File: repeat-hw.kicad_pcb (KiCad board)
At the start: 2 copper layers, 1 part, among them U1 nRF5340-QKxx

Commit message: added W5100
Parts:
- added J1: RB1-125BAG1A, Connector_RJ:RJ45_Cetus_J1B1211CCD_Horizontal, F.Cu at (79.7, 53.6)
- added U2: W5100, Package_QFP:LQFP-80_10x10mm_P0.4mm, F.Cu at (83.0, 40.0)
- added Y1: 32MHz, Crystal:Crystal_SMD_3225-4Pin_3.2x2.5mm, F.Cu at (107.9, 35.0)
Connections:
- U1 pad A13: unconnected-(U1-PadA13) -> Net-(C14-Pad1)
- U1 pad A15: unconnected-(U1-PadA15) -> Net-(C12-Pad1)
- U1 pad A21: unconnected-(U1-PadA21) -> Net-(L1-Pad2)
- U1 pad A23: unconnected-(U1-PadA23) -> Net-(C8-Pad1)
- U1 pad A27: unconnected-(U1-PadA27) -> Net-(C11-Pad1)
- U1 pad A5: unconnected-(U1-PadA5) -> Net-(C1-Pad1)
- U1 pad AA1: unconnected-(U1-PadAA1) -> /MCU/NFC2
- U1 pad AC31: unconnected-(U1-PadAC31) -> Net-(C10-Pad1)
- U1 pad B10: unconnected-(U1-PadB10) -> Net-(L3-Pad2)
- U1 pad B2: unconnected-(U1-PadB2) -> /MCU/D+
- U1 pad B30: unconnected-(U1-PadB30) -> Net-(C9-Pad1)
- U1 pad B4: unconnected-(U1-PadB4) -> /MCU/D-
- U1 pad B6: unconnected-(U1-PadB6) -> Net-(C3-Pad1)
- U1 pad C31: unconnected-(U1-PadC31) -> Net-(C4-Pad1)
- U1 pad E1: unconnected-(U1-PadE1) -> VDD
- U1 pad EP: unconnected-(U1-PadEP) -> GND
- U1 pad G31: unconnected-(U1-PadG31) -> Net-(C11-Pad1)
- U1 pad L31: unconnected-(U1-PadL31) -> Net-(C13-Pad1)
- U1 pad W1: unconnected-(U1-PadW1) -> /MCU/NFC1

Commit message: Finishe PoE and ethernet
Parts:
- removed J1: RB1-125BAG1A, Connector_RJ:RJ45_Cetus_J1B1211CCD_Horizontal
- added C1: 4u7, Connector_RJ:RJ45_Cetus_J1B1211CCD_Horizontal, F.Cu at (77.7, 63.0)
- added D2: 1N4148W, Diode_SMD:D_SOD-123, F.Cu at (112.7, 59.5)
- added U3: TLV431DBZ, Package_TO_SOT_SMD:SOT-23, F.Cu at (118.0, 60.0)
- added Y2: 25MHz, Crystal:Crystal_SMD_3225-4Pin_3.2x2.5mm, F.Cu at (112.4, 63.4)
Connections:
- net Net-(U2-Pad10) renamed GNDA
- net Net-(U2-Pad12) renamed +3V3
- net Net-(U2-Pad7) renamed +1V8A
- U2 pad 1: unconnected-(U2-Pad1) -> Net-(U2-Pad1)
- U2 pad 11: unconnected-(U2-Pad11) -> +1V8
- U2 pad 13: Net-(U2-Pad13) -> GND
- U2 pad 14: Net-(U2-Pad13) -> GND
- U2 pad 15: Net-(U2-Pad15) -> +1V8
- U2 pad 16: Net-(U2-Pad15) -> +1V8
- U2 pad 17: Net-(U2-Pad13) -> GND
- U2 pad 2: unconnected-(U2-Pad2) -> +3V3A
- U2 pad 27: unconnected-(U2-Pad27) -> /W5100 + PoE/MISO
- U2 pad 28: unconnected-(U2-Pad28) -> /W5100 + PoE/MOSI
- U2 pad 29: unconnected-(U2-Pad29) -> /W5100 + PoE/~{CS}
- U2 pad 30: unconnected-(U2-Pad30) -> /W5100 + PoE/CLK
- U2 pad 31: unconnected-(U2-Pad31) -> Net-(U2-Pad31)
- U2 pad 32: Net-(U2-Pad13) -> GND
- U2 pad 33: Net-(U2-Pad15) -> +1V8
- U2 pad 34: unconnected-(U2-Pad34) -> GND
- U2 pad 35: unconnected-(U2-Pad35) -> GND
- U2 pad 36: unconnected-(U2-Pad36) -> GND
- U2 pad 37: unconnected-(U2-Pad37) -> GND
- U2 pad 43: Net-(U2-Pad13) -> GND
- U2 pad 5: unconnected-(U2-Pad5) -> /W5100 + PoE/RD+
- U2 pad 56: unconnected-(U2-Pad56) -> /W5100 + PoE/~{INT}
- U2 pad 59: unconnected-(U2-Pad59) -> /W5100 + PoE/~{RST}
- U2 pad 6: unconnected-(U2-Pad6) -> /W5100 + PoE/RD-
- U2 pad 63: unconnected-(U2-Pad63) -> GND
- U2 pad 64: unconnected-(U2-Pad64) -> GND
- U2 pad 65: unconnected-(U2-Pad65) -> GND
- U2 pad 66: unconnected-(U2-Pad66) -> /W5100 + PoE/LINK
- U2 pad 68: Net-(U2-Pad13) -> GND
- U2 pad 69: Net-(U2-Pad15) -> +1V8
- U2 pad 70: unconnected-(U2-Pad70) -> /W5100 + PoE/FDX
- U2 pad 75: unconnected-(U2-Pad75) -> Net-(U2-Pad75)
- U2 pad 76: unconnected-(U2-Pad76) -> Net-(U2-Pad76)
- U2 pad 8: unconnected-(U2-Pad8) -> /W5100 + PoE/TD+
- U2 pad 9: unconnected-(U2-Pad9) -> /W5100 + PoE/TD-

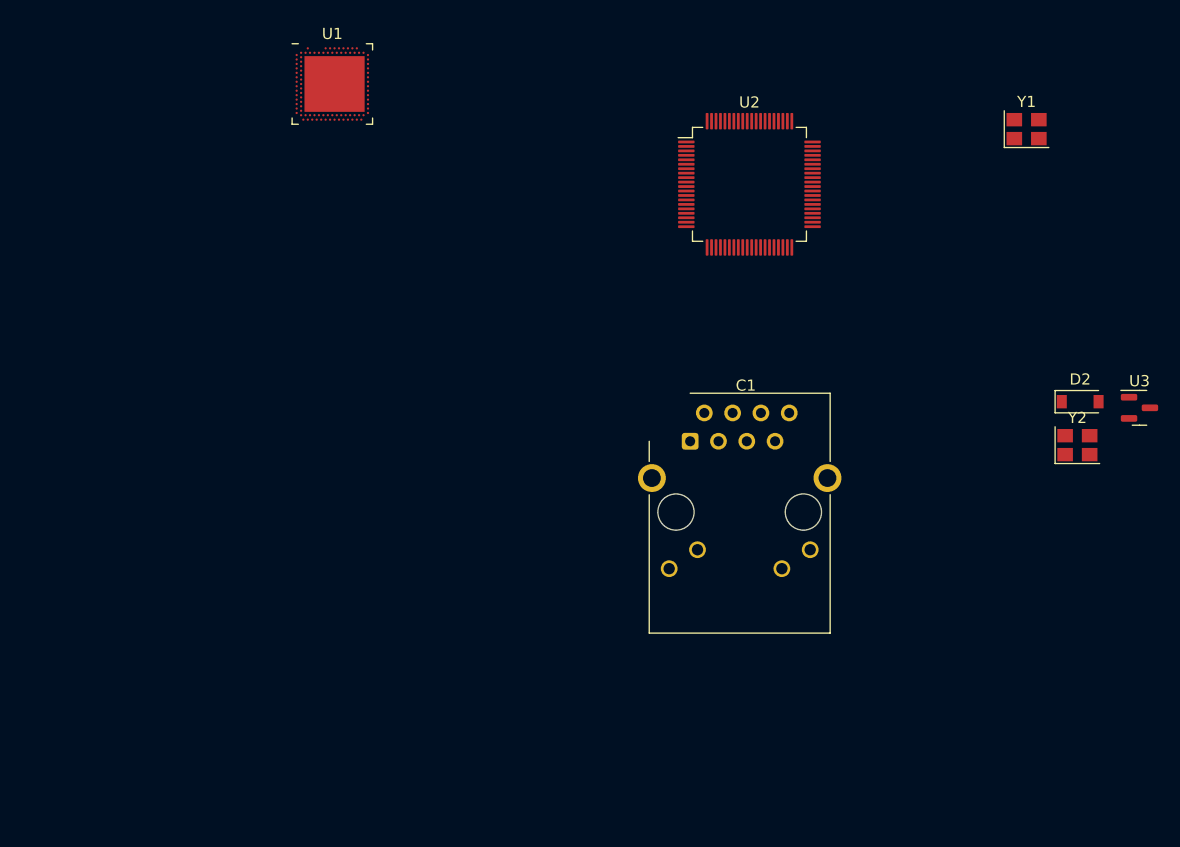
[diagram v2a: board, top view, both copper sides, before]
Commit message: Added USB port
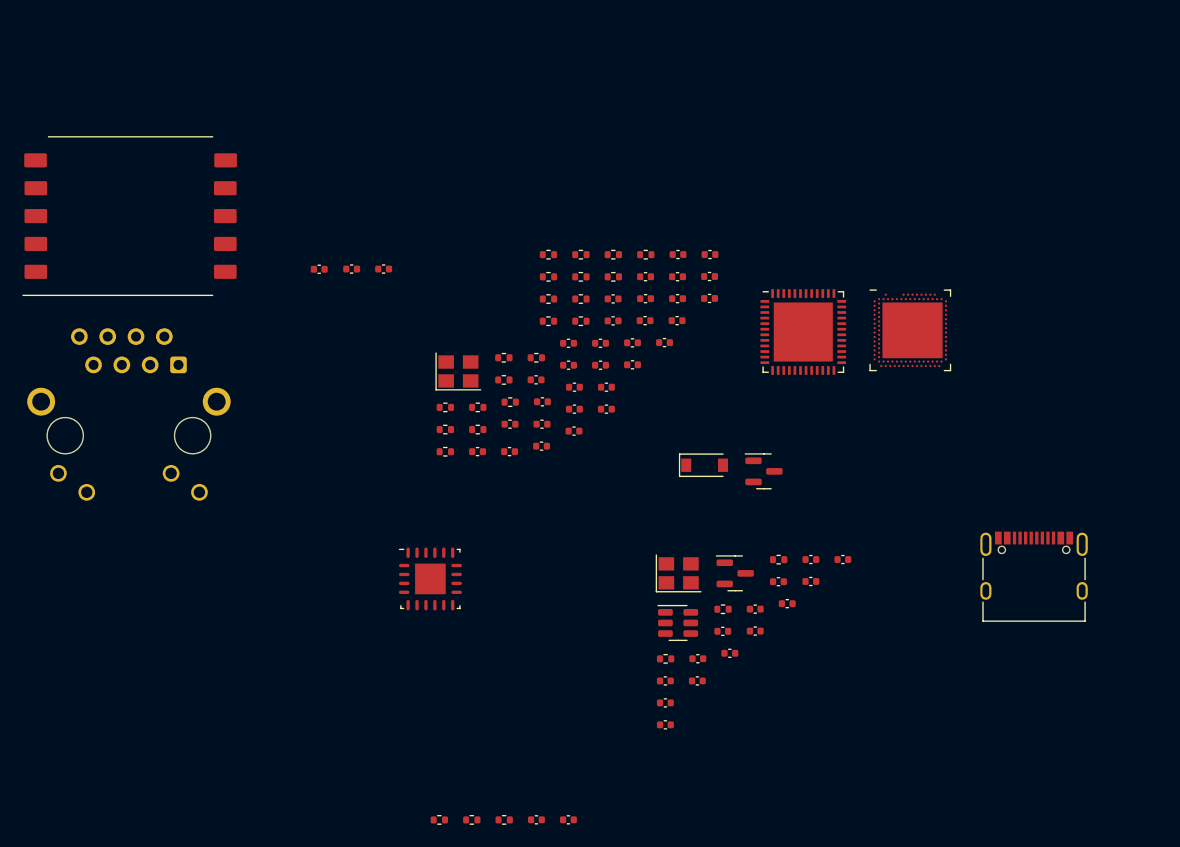
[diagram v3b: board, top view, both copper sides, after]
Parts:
- added C10: 100n, Capacitor_SMD:C_0402_1005Metric, F.Cu at (63.9, 97.0)
- added C11: 2n2, Capacitor_SMD:C_0402_1005Metric, F.Cu at (83.5, 80.1)
- added C13: 0p7, Capacitor_SMD:C_0402_1005Metric, F.Cu at (85.6, 75.7)
- added C15: 100n, Capacitor_SMD:C_0402_1005Metric, F.Cu at (78.4, 82.6)
- added C16: 100n, Capacitor_SMD:C_0402_1005Metric, F.Cu at (75.5, 86.5)
- added C17: 100n, Capacitor_SMD:C_0402_1005Metric, F.Cu at (83.5, 78.1)
- added C18: 100n, Capacitor_SMD:C_0402_1005Metric, F.Cu at (80.6, 80.1)
- added C19: 100n, Capacitor_SMD:C_0402_1005Metric, F.Cu at (91.4, 73.7)
- added C2: 1u, Capacitor_SMD:C_0402_1005Metric, F.Cu at (78.3, 84.5)
- added C20: 100n, Capacitor_SMD:C_0402_1005Metric, F.Cu at (66.8, 97.0)
- added C21: 100n, Capacitor_SMD:C_0402_1005Metric, F.Cu at (88.5, 73.7)
- added C22: 100n, Capacitor_SMD:C_0402_1005Metric, F.Cu at (75.5, 88.5)
- added C24: 10p, Capacitor_SMD:C_0402_1005Metric, F.Cu at (47.3, 47.6)
- added C25: 10p, Capacitor_SMD:C_0402_1005Metric, F.Cu at (64.4, 63.5)
- added C30: 10n, Capacitor_SMD:C_0402_1005Metric, F.Cu at (61.5, 64.0)
- added C31: 10u, Capacitor_SMD:C_0402_1005Metric, F.Cu at (64.5, 59.5)
- added C32: 1u, Capacitor_SMD:C_0402_1005Metric, F.Cu at (63.9, 57.5)
- added C33: 1u, Capacitor_SMD:C_0402_1005Metric, F.Cu at (69.7, 56.2)
- added C34: 10n, Capacitor_SMD:C_0402_1005Metric, F.Cu at (73.7, 48.3)
- added C35: 1u, Capacitor_SMD:C_0402_1005Metric, F.Cu at (79.4, 48.3)
- added C36: 100n, Capacitor_SMD:C_0402_1005Metric, F.Cu at (64.4, 61.5)
- added C37: 100n, Capacitor_SMD:C_0402_1005Metric, F.Cu at (50.2, 47.6)
- added C38: 100n, Capacitor_SMD:C_0402_1005Metric, F.Cu at (76.6, 50.3)
- added C39: 100n, Capacitor_SMD:C_0402_1005Metric, F.Cu at (58.6, 64.0)
- added C4: 10p, Capacitor_SMD:C_0402_1005Metric, F.Cu at (81.3, 82.1)
- added C40: 100n, Capacitor_SMD:C_0402_1005Metric, F.Cu at (72.5, 56.2)
- added C41: 100n, Capacitor_SMD:C_0402_1005Metric, F.Cu at (76.5, 52.2)
- added C42: 100n, Capacitor_SMD:C_0402_1005Metric, F.Cu at (67.3, 60.2)
- added C43: 100n, Capacitor_SMD:C_0402_1005Metric, F.Cu at (70.8, 52.2)
- added C44: 1n, Capacitor_SMD:C_0402_1005Metric, F.Cu at (61.5, 61.5)
- added C45: 1n, Capacitor_SMD:C_0402_1005Metric, F.Cu at (66.8, 56.2)
- added C48: 1n, Capacitor_SMD:C_0402_1005Metric, F.Cu at (70.2, 60.2)
- added C49: 1n, Capacitor_SMD:C_0402_1005Metric, F.Cu at (44.4, 47.6)
- added C50: 1n, Capacitor_SMD:C_0402_1005Metric, F.Cu at (73.7, 50.3)
- added C51: 1n, Capacitor_SMD:C_0402_1005Metric, F.Cu at (75.4, 54.2)
- added C53: 100n, Capacitor_SMD:C_0402_1005Metric, F.Cu at (79.5, 46.3)
- added C54: 1n, Capacitor_SMD:C_0402_1005Metric, F.Cu at (76.6, 46.3)
- added C55: 1n, Capacitor_SMD:C_0402_1005Metric, F.Cu at (72.5, 54.2)
- added C56: 100n, Capacitor_SMD:C_0402_1005Metric, F.Cu at (67.3, 62.1)
- added C57: 100n, Capacitor_SMD:C_0402_1005Metric, F.Cu at (79.4, 50.2)
- added C58: 100n, Capacitor_SMD:C_0402_1005Metric, F.Cu at (70.2, 58.2)
- added C59: 1u, Capacitor_SMD:C_0402_1005Metric, F.Cu at (73.7, 52.2)
- added C60: 100n, Capacitor_SMD:C_0402_1005Metric, F.Cu at (67.3, 58.2)
- added C8: 100n, Capacitor_SMD:C_0402_1005Metric, F.Cu at (86.4, 77.6)
- added C9: 10p, Capacitor_SMD:C_0402_1005Metric, F.Cu at (75.5, 84.5)
- added D1: BAV99, Package_TO_SOT_SMD:SOT-23, F.Cu at (81.7, 74.9)
- added FB1: 1u, Capacitor_SMD:C_0402_1005Metric, F.Cu at (66.8, 54.3)
- added FB2: 1u, Capacitor_SMD:C_0402_1005Metric, F.Cu at (69.7, 54.3)
- added FB3: 1u, Capacitor_SMD:C_0402_1005Metric, F.Cu at (70.8, 50.3)
- added J1: USB_C_Receptacle_USB2.0, Connector_USB:USB_C_Receptacle_XKB_U262-16XN-4BVC11, F.Cu at (108.5, 75.4)
- added L2: 2n2, Capacitor_SMD:C_0402_1005Metric, F.Cu at (88.5, 75.6)
- added L4: 1u, Capacitor_SMD:C_0402_1005Metric, F.Cu at (76.6, 48.3)
- added R1: 2R2, Resistor_SMD:R_0402_1005Metric, F.Cu at (58.1, 97.0)
- added R10: 12k1, Resistor_SMD:R_0402_1005Metric, F.Cu at (67.9, 48.3)
- added R11: 2k2, Resistor_SMD:R_0402_1005Metric, F.Cu at (55.7, 64.0)
- added R12: 300R 1%, Resistor_SMD:R_0402_1005Metric, F.Cu at (61.0, 55.6)
- added R13: 12k 1%, Resistor_SMD:R_0402_1005Metric, F.Cu at (58.6, 60.0)
- added R14: 5k1, Resistor_SMD:R_0402_1005Metric, F.Cu at (67.9, 50.3)
- added R15: 24k3, Resistor_SMD:R_0402_1005Metric, F.Cu at (65.0, 50.3)
- added R16: 48R7, Resistor_SMD:R_0402_1005Metric, F.Cu at (55.7, 60.0)
- added R17: 3R3, Resistor_SMD:R_0402_1005Metric, F.Cu at (70.8, 48.3)
- added R18: 3R3, Resistor_SMD:R_0402_1005Metric, F.Cu at (55.7, 62.0)
- added R19: 3R3, Resistor_SMD:R_0402_1005Metric, F.Cu at (61.6, 59.5)
- added R2: 10k, Resistor_SMD:R_0402_1005Metric, F.Cu at (75.5, 82.6)
- added R20: 3R3, Resistor_SMD:R_0402_1005Metric, F.Cu at (58.6, 62.0)
- added R21: 49R9, Resistor_SMD:R_0402_1005Metric, F.Cu at (65.0, 52.3)
- added R22: 49R9, Resistor_SMD:R_0402_1005Metric, F.Cu at (67.9, 46.3)
- added R23: 49R9, Resistor_SMD:R_0402_1005Metric, F.Cu at (65.0, 48.3)
- added R24: 49R9, Resistor_SMD:R_0402_1005Metric, F.Cu at (73.7, 46.3)
- added R25: 330R, Resistor_SMD:R_0402_1005Metric, F.Cu at (65.0, 46.3)
- added R26: 330R, Resistor_SMD:R_0402_1005Metric, F.Cu at (70.8, 46.3)
- added R3: R, Resistor_SMD:R_0402_1005Metric, F.Cu at (55.2, 97.0)
- added R4: R, Resistor_SMD:R_0402_1005Metric, F.Cu at (61.0, 97.0)
- added R5: R, Resistor_SMD:R_0402_1005Metric, F.Cu at (80.7, 78.1)
- added R6: R, Resistor_SMD:R_0402_1005Metric, F.Cu at (85.6, 73.7)
- added R7: 1M, Resistor_SMD:R_0402_1005Metric, F.Cu at (61.0, 57.5)
- added R8: 10k, Resistor_SMD:R_0402_1005Metric, F.Cu at (67.9, 52.3)
- added R9: 36k5, Resistor_SMD:R_0402_1005Metric, F.Cu at (63.9, 55.6)
- added T1: FA2805, coilcraft:Transformer_Coilcraft_Si3402, F.Cu at (27.5, 42.9)
- added U3: W5100S, Package_DFN_QFN:QFN-48-1EP_7x7mm_P0.5mm_EP5.3x5.3mm, F.Cu at (87.8, 53.2)
- added U6: SI3402, skyworks:Skyworks_QFN-20_1EP5x5mm_P0.8mm_EP2.7x2.7mm, F.Cu at (54.4, 75.4)
- C1: moved to B.Cu
- U2: value W5100 -> USBLC6-2SC6; footprint Package_QFP:LQFP-80_10x10mm_P0.4mm -> Package_TO_SOT_SMD:SOT-23-6
- moved U1 56.4 mm to (97.5, 53.1)
- moved Y2 55.9 mm to (56.9, 56.8)
- moved Y1 50.6 mm to (76.7, 74.9)
- moved C1 46.4 mm to (31.8, 56.2), turned to 180 degrees
- moved U2 39.9 mm to (76.6, 79.3)
- moved U4 34.2 mm to (84.3, 65.8)
- moved D5 34.2 mm to (79.0, 65.2)
- renumbered D2 to D5, U3 to U4
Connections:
- net /MCU/NFC1 renamed /NFC1
- net /MCU/NFC2 renamed /NFC2
- U1 pad A19: VDD -> +3V3
- U1 pad AA31: unconnected-(U1-PadAA31) -> /SWDIO
- U1 pad AC1: VDD -> +3V3
- U1 pad AC31: Net-(C10-Pad1) -> /~{RESET}
- U1 pad AG1: VDD -> +3V3
- U1 pad AH2: unconnected-(U1-PadAH2) -> /SPIM_CLK
- U1 pad AJ1: unconnected-(U1-PadAJ1) -> /SPIM_MOSI
- U1 pad AK2: unconnected-(U1-PadAK2) -> /SPIM_MISO
- U1 pad AK4: unconnected-(U1-PadAK4) -> /~{SPIM_CS}
- U1 pad AL11: VDD -> +3V3
- U1 pad AL17: VDD -> +3V3
- U1 pad AL25: VDD -> +3V3
- U1 pad AL3: VDD -> +3V3
- U1 pad AL5: unconnected-(U1-PadAL5) -> /~{INT}
- U1 pad AL7: VDD -> +3V3
- U1 pad B2: /MCU/D+ -> /D+
- U1 pad B28: VDD -> +3V3
- U1 pad B4: /MCU/D- -> /D-
- U1 pad B8: VDD -> +3V3
- U1 pad C1: VDD -> +3V3
- U1 pad E1: VDD -> +3V3
- U1 pad E31: VDD -> +3V3
- U1 pad L1: VDD -> +3V3
- U1 pad N31: VDD -> +3V3
- U1 pad U1: VDD -> +3V3
- U1 pad W31: unconnected-(U1-PadW31) -> /SWDCLK
- U2 pad 1: Net-(U2-Pad1) -> /D+
- U2 pad 2: +3V3A -> GND
- U2 pad 3: unconnected-(U2-Pad3) -> /D-
- U2 pad 4: GNDA -> Net-(J1-PadA7)
- U2 pad 5: /W5100 + PoE/RD+ -> VBUS
- U2 pad 6: /W5100 + PoE/RD- -> Net-(J1-PadA6)
- Y2 pad 1: Net-(U2-Pad75) -> Net-(C25-Pad1)
- Y2 pad 3: Net-(U2-Pad76) -> Net-(C24-Pad1)

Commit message: Polished schematic
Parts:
- removed C58: 100n, Capacitor_SMD:C_0402_1005Metric
- removed FB3: 1u, Capacitor_SMD:C_0402_1005Metric
- added AE1: SWRA117D, RF_Antenna:Texas_SWRA117D_2.4GHz_Left, F.Cu at (61.5, 25.4)
- added C12: 1u, Capacitor_SMD:C_0603_1608Metric, F.Cu at (117.0, 60.0)
- added C14: 1u, Capacitor_SMD:C_0603_1608Metric, F.Cu at (121.2, 57.1)
- added C23: 100n, Capacitor_SMD:C_0402_1005Metric, F.Cu at (128.7, 56.1)
- added C26: 470u, Capacitor_Tantalum_SMD:CP_EIA-2012-12_Kemet-R, F.Cu at (129.2, 41.5)
- added C27: 100u, Capacitor_SMD:C_1206_3216Metric, F.Cu at (124.1, 41.7)
- added C28: 1n 3kV, Capacitor_SMD:C_1206_3216Metric, F.Cu at (133.4, 28.4)
- added C29: 1n 3kV, Capacitor_SMD:C_1206_3216Metric, F.Cu at (139.0, 28.4)
- added C3: 4u7, Capacitor_SMD:C_0603_1608Metric, F.Cu at (121.0, 60.0)
- added C46: 3u3, Capacitor_SMD:C_0603_1608Metric, F.Cu at (142.2, 31.3)
- added C47: 3u3, Capacitor_SMD:C_0603_1608Metric, F.Cu at (143.8, 28.0)
- added C5: DNP, Capacitor_SMD:C_0402_1005Metric, F.Cu at (132.7, 51.1)
- added C52: 10u, Capacitor_SMD:C_0603_1608Metric, F.Cu at (150.2, 23.5)
- added C6: 1u, Capacitor_SMD:C_0603_1608Metric, F.Cu at (130.3, 48.8)
- added C61: 1n 3kV, Capacitor_SMD:C_1206_3216Metric, F.Cu at (118.5, 41.7)
- added C62: 1p, Capacitor_SMD:C_0402_1005Metric, F.Cu at (50.1, 27.3)
- added C63: 1p, Capacitor_SMD:C_0402_1005Metric, F.Cu at (50.1, 29.3)
- added C64: 2p, Capacitor_SMD:C_0402_1005Metric, F.Cu at (66.7, 26.5)
- added C65: 2p, Capacitor_SMD:C_0402_1005Metric, F.Cu at (52.9, 27.3)
- added C66: 100n, Capacitor_SMD:C_0402_1005Metric, F.Cu at (58.7, 29.3)
- added C67: 10u, Capacitor_SMD:C_0402_1005Metric, F.Cu at (55.8, 29.3)
- added C68: 1p, Capacitor_SMD:C_0402_1005Metric, F.Cu at (129.8, 53.1)
- added C69: 470p, Capacitor_SMD:C_0402_1005Metric, F.Cu at (135.8, 40.0)
- added C7: 100n, Capacitor_SMD:C_0402_1005Metric, F.Cu at (124.4, 59.3)
- added C70: 1u, Capacitor_SMD:C_0603_1608Metric, F.Cu at (126.3, 48.8)
- added C71: 1u, Capacitor_SMD:C_0603_1608Metric, F.Cu at (126.3, 51.4)
- added C72: 1u, Capacitor_SMD:C_0603_1608Metric, F.Cu at (125.2, 56.4)
- added C73: 100n, Capacitor_SMD:C_0402_1005Metric, F.Cu at (132.9, 42.0)
- added C74: 100n, Capacitor_SMD:C_0402_1005Metric, F.Cu at (153.6, 22.1)
- added C75: 100n, Capacitor_SMD:C_0402_1005Metric, F.Cu at (156.5, 20.2)
- added C76: 100n, Capacitor_SMD:C_0402_1005Metric, F.Cu at (140.0, 36.6)
- added D2: PMEG3010EJ, Diode_SMD:D_SOD-323F, F.Cu at (121.6, 53.5)
- added D3: PMEG3010EJ, Diode_SMD:D_SOD-323F, F.Cu at (117.1, 57.3)
- added D4: BAV99, Package_TO_SOT_SMD:SOT-23, F.Cu at (121.9, 49.8)
- added D6: DFLT30A, Diode_SMD:D_PowerDI-123, F.Cu at (112.6, 41.9)
- added D7: PMEG045T100EPD, Package_TO_SOT_SMD:Nexperia_CFP15_SOT-1289, F.Cu at (147.9, 19.4)
- added FB4: 330R, Inductor_SMD:L_0805_2012Metric, F.Cu at (138.0, 31.4)
- added FB5: 330R, Inductor_SMD:L_0805_2012Metric, F.Cu at (145.9, 23.6)
- added FB6: 330R, Inductor_SMD:L_0805_2012Metric, F.Cu at (154.4, 17.8)
- added FB7: 330R, Inductor_SMD:L_0805_2012Metric, F.Cu at (138.0, 34.2)
- added J2: ARJM11C7-114-BA-EW2, abracon:ARJM11C7-114-BA-EW2, F.Cu at (120.1, 28.1)
- added J3: Conn_Coaxial, Connector_Coaxial:U.FL_Hirose_U.FL-R-SMT-1_Vertical, F.Cu at (112.1, 58.9)
- added L5: 3n, Capacitor_SMD:C_0402_1005Metric, F.Cu at (61.5, 27.3)
- added L6: 3n, Capacitor_SMD:C_0402_1005Metric, F.Cu at (58.7, 27.3)
- added L7: 1n9, Capacitor_SMD:C_0402_1005Metric, F.Cu at (55.8, 27.3)
- added L8: 1n9, Capacitor_SMD:C_0402_1005Metric, F.Cu at (52.9, 29.3)
- added R27: 10R, Resistor_SMD:R_0402_1005Metric, F.Cu at (137.2, 36.6)
- added R28: R, Resistor_SMD:R_0402_1005Metric, F.Cu at (141.7, 33.6)
- added R29: 49R9, Resistor_SMD:R_0402_1005Metric, F.Cu at (153.6, 20.2)
- added U10: USBLC6-2SC6, Package_TO_SOT_SMD:SOT-23-6, F.Cu at (133.1, 32.3)
- added U11: USBLC6-2SC6, Package_TO_SOT_SMD:SOT-23-6, F.Cu at (133.1, 36.8)
- added U5: VO618A, Package_SO:SO-4_7.6x3.6mm_P2.54mm, F.Cu at (137.1, 19.0)
- added U7: nRF21540, Package_DFN_QFN:QFN-16-1EP_4x4mm_P0.65mm_EP2.7x2.7mm_ThermalVias, F.Cu at (68.4, 22.4)
- added U8: VO618A, Package_SO:SO-4_7.6x3.6mm_P2.54mm, F.Cu at (137.1, 24.1)
- added U9: AMS1117-3.3, Package_TO_SOT_SMD:SOT-223-3_TabPin2, F.Cu at (114.5, 51.7)
- C1: footprint Connector_RJ:RJ45_Cetus_J1B1211CCD_Horizontal -> Capacitor_SMD:C_0603_1608Metric
- C2: value 1u -> 100n
- C32, C33, C35, C59, L4: footprint Capacitor_SMD:C_0402_1005Metric -> Capacitor_SMD:C_0603_1608Metric
- C34: value 10n -> 15n
- C57: value 100n -> 10u; footprint Capacitor_SMD:C_0402_1005Metric -> Capacitor_SMD:C_0603_1608Metric
- FB1, FB2: value 1u -> TBD
- R10: value 12k1 -> 12k1 1%
- R14: value 5k1 -> 4k99 1%
- R15: value 24k3 -> 24k3 1%
- R16: value 48R7 -> 75R 1%
- R21: value 49R9 -> 180k
- R3: value R -> 100k
- R4: value R -> 180k
- R5, R6: value R -> 5k1
- R8: value 10k -> 100k
- R9: value 36k5 -> 36k5 1%
- moved R23 98.1 mm to (158.2, 17.4)
- moved R24 78.6 mm to (149.6, 25.8)
- moved R21 68.9 mm to (133.8, 48.6)
- moved R22 65.3 mm to (132.9, 40.0)
- moved R8 61.9 mm to (129.8, 51.1)
- moved C2 51.6 mm to (124.4, 61.3)
- moved C57 46.4 mm to (125.7, 53.9)
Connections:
- C2 pad 1: +3V3 -> /USENSE_POE
- C53 pad 2: GNDA -> GND
- C56 pad 2: GNDA -> GND
- C57 pad 1: Net-(C57-Pad1) -> +5V
- J1 pad A6: Net-(J1-PadA6) -> /D+
- J1 pad A7: Net-(J1-PadA7) -> /D-
- J1 pad B6: Net-(J1-PadA6) -> /D+
- J1 pad B7: Net-(J1-PadA7) -> /D-
- R17 pad 1: /W5100 + PoE/RD- -> /W5100 + PoE/ESD_RD-
- R17 pad 2: Net-(J2-Pad3) -> /W5100 + PoE/RD-
- R18 pad 1: /W5100 + PoE/RD+ -> /W5100 + PoE/ESD_RD+
- R18 pad 2: Net-(J2-Pad5) -> /W5100 + PoE/RD+
- R19 pad 1: /W5100 + PoE/TD- -> /W5100 + PoE/ESD_TD-
- R19 pad 2: Net-(J2-Pad8) -> /W5100 + PoE/TD-
- R20 pad 1: /W5100 + PoE/TD+ -> /W5100 + PoE/ESD_TD+
- R20 pad 2: Net-(J2-Pad10) -> /W5100 + PoE/TD+
- R21 pad 1: Net-(J2-Pad3) -> /USENSE_POE
- R21 pad 2: Net-(C57-Pad1) -> GND
- R22 pad 1: Net-(J2-Pad5) -> /W5100 + PoE/RD-
- R22 pad 2: Net-(C57-Pad1) -> Net-(C73-Pad1)
- R23 pad 1: Net-(J2-Pad8) -> /W5100 + PoE/RD+
- R23 pad 2: Net-(C58-Pad1) -> Net-(C73-Pad1)
- R24 pad 1: Net-(J2-Pad10) -> /W5100 + PoE/TD-
- R24 pad 2: Net-(C58-Pad1) -> Net-(C74-Pad1)
- R8 pad 1: +3V3 -> /W5100 + PoE/5V
- R8 pad 2: /~{RESET} -> /USENSE_POE
- U1 pad B2: /D+ -> /ESD_D+
- U1 pad B4: /D- -> /ESD_D-
- U2 pad 1: /D+ -> /ESD_D+
- U2 pad 3: /D- -> /ESD_D-
- U2 pad 4: Net-(J1-PadA7) -> /D-
- U2 pad 6: Net-(J1-PadA6) -> /D+
- U6 pad 15: Net-(C31-Pad2) -> unconnected-(U6-Pad15)
- U6 pad 5: (no net) -> Net-(U6-Pad5)
